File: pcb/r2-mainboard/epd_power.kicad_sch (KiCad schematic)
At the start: 79 parts, among them Q1 AO3401A, Q2 S8050, Q6 AO3400A, Q7 AO3401A, Q8 AO3401A, U23 LGS6302B5, U24 LGS6302B5, U26 LGS5145, U31 LM321, U6 MT9700, U7 TPS22914BYFPR, U8 TPS22914BYFPR, U9 LGS5145

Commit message: R2: the six approved edits, and one of them was already done
Owner-approved 2026-08-19, KiCad closed for the pass.

1. R225 22k -> 20.5K/1%, LCSC C57105 (0402WGF2052TCE, UNI-ROYAL, the
   family the rest of the board already uses). Rendered and checked:
   R224 390k over R225 20.5k with R213 100k injecting VGH_DAC, so
   20.5||100 = 17.01k and VGH = 1.2 x (1 + 390/17.01) = 28.71 V at
   DAC = 0 -- exactly epd-port.md 10.3's target.
2. The five sense-divider caps that carried codes for the wrong
   capacitance -> C1523 (0402B102K500NT, 1 nF 50 V X7R, JLC Basic,
   5.3 M stock). One part covers both the 25 V and 50 V positions.
2b. R88/R224 -> C54920667 (HRC0402F3903DNTO, 390k 1%, 20 k stock).
   C25782 had 14 units against two per board. The owner found this one;
   both obvious alternatives were traps -- C23150 is 0603, and C44937
   is 3.9 ohm despite "390K" in its part number.
3. C147 set DNP rather than deleted. panel.md 7 had already ruled that
   J6.7/J6.44 stay; that covered the pins but not the capacitor on the
   dead net. DNP drops it from placement, keeps the topology of a frozen
   sheet untouched, and leaves the footprint if a future panel drives
   the rail. in_bom stays yes -- that is this board's convention for all
   13 DNP parts, so they show up flagged rather than vanishing.
4. Ten duplicate #PWR references renumbered to #PWR1112-1121 on the
   battery sheet, which was the colliding side in every case.
5. J3 was already deleted on 2026-08-15. No work needed.
6. Specter -> Reflow across 22 files: 14 sheets, 7 generators, the
   project file. .history/ deliberately untouched.

Verified as one change: netlist before and after has 518 nets with
identical pin membership, and epd_power and epd were rendered to PNG and
inspected.

Docs updated to match: epd-port.md 10 is applied rather than designed,
frontlight.md 1 loses the "9 in series is inferred" hedge (the vendor
listing confirms 2 x 9), and io-expansion.md 4's "only guess on this
sheet" is resolved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
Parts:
- R224, R88: LCSC C25782 -> C54920667; MPN 0402WGF3903TCE -> HRC0402F3903DNTO; Manufacturer UNI-ROYAL -> HWA CHN
- R225: value 22K/1% -> 20.5K/1%; LCSC C25768 -> C57105; MPN 0402WGF2202TCE -> 0402WGF2052TCE
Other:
- title: Glider-R2 / Specter mainboard -> Glider-R2 / Reflow mainboard
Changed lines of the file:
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@@
 	(paper "A4")
 	(title_block
-		(title "Glider-R2 / Specter mainboard")
+		(title "Glider-R2 / Reflow mainboard")
 		(date "2026-08-07")
 		(rev "A")
@@
 			)
 		)
-		(property "LCSC" "C25782"
+		(property "LCSC" "C54920667"
 			(at 139.7 80.01 0)
 			(hide yes)
@@
 			)
 		)
-		(property "Manufacturer" "UNI-ROYAL"
+		(property "Manufacturer" "HWA CHN"
 			(at 0 0 0)
 			(hide yes)
@@
 			)
 		)
-		(property "MPN" "0402WGF3903TCE"
+		(property "MPN" "HRC0402F3903DNTO"
 			(at 0 0 0)
 			(hide yes)
@@
 			)
 		)
-		(property "LCSC" "C25782"
+		(property "LCSC" "C54920667"
 			(at 137.16 115.57 0)
 			(hide yes)
@@
 			)
 		)
-		(property "Manufacturer" "UNI-ROYAL"
+		(property "Manufacturer" "HWA CHN"
 			(at 0 0 0)
 			(hide yes)
@@
 			)
 		)
-		(property "MPN" "0402WGF3903TCE"
+		(property "MPN" "HRC0402F3903DNTO"
 			(at 0 0 0)
 			(hide yes)
@@
 			)
 		)
-		(property "Value" "22K/1%"
+		(property "Value" "20.5K/1%"
 			(at 142.24 124.46 0)
 			(show_name no)
@@
 			)
 		)
-		(property "LCSC" "C25768"
+		(property "LCSC" "C57105"
 			(at 137.16 123.19 0)
 			(hide yes)
@@
 			)
 		)
-		(property "MPN" "0402WGF2202TCE"
+		(property "MPN" "0402WGF2052TCE"
 			(at 0 0 0)
 			(hide yes)

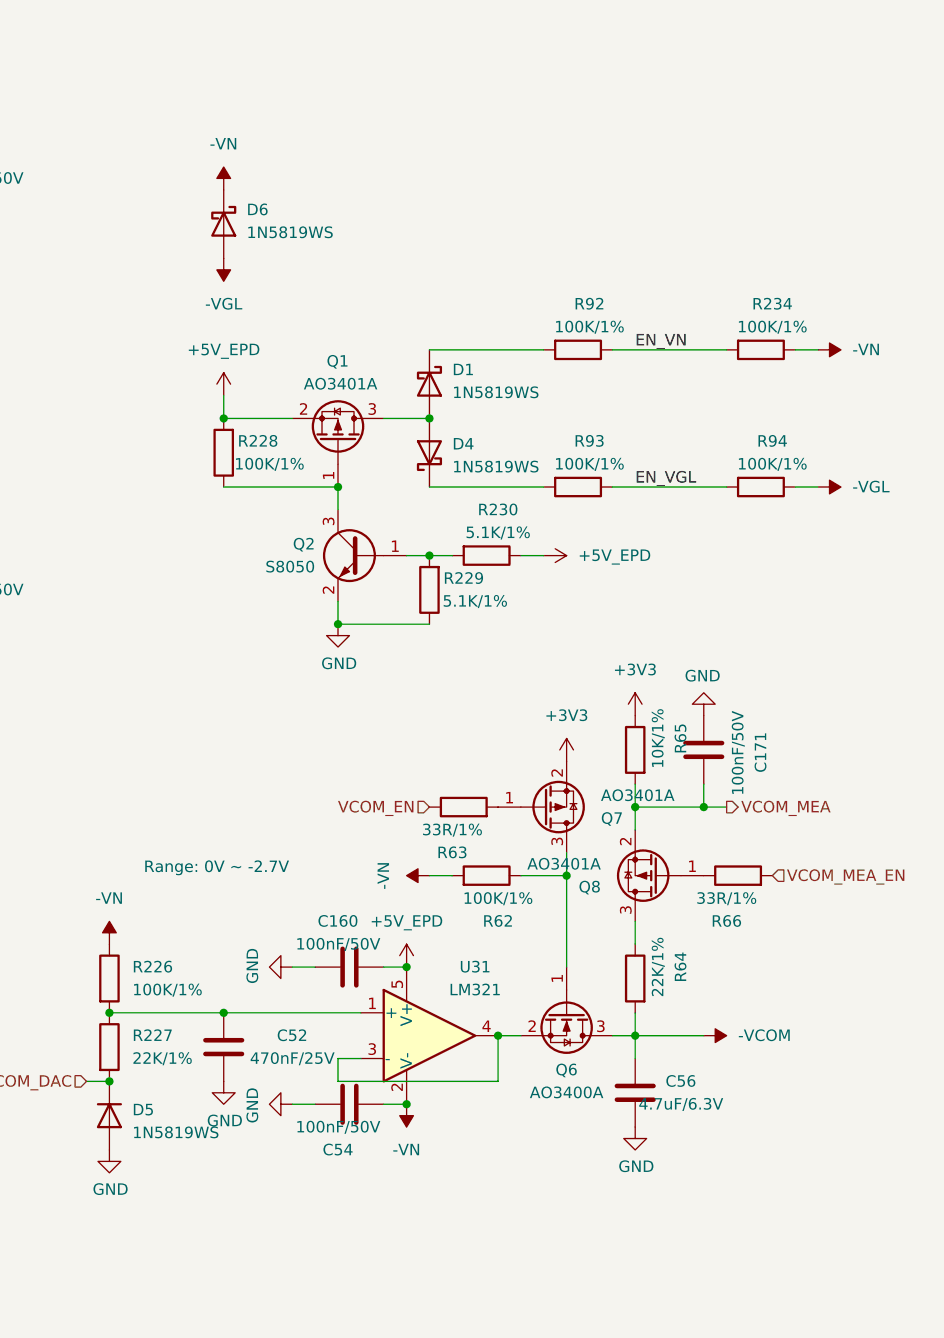
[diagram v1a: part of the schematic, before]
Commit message: Touch decided: I2C hand-wired for the prototype; Caster bitgen applied
Good Display's answer of 2026-08-31 closes the on-board GT9110H idea:
the driving board is another customer's design and they will not share
files, so the panel's ITO channel map is unobtainable at prototype
scale. The production path is now priced instead -- US$750 tooling,
MOQ 1000/lot, for a custom panel with the interface and touch IC of our
choosing.

Owner's decision: option C. Touch runs over I2C on J22, hand-wired to
the vendor board's test points for the prototype. USB was rejected --
USB0 is the charge port and USB1 is now the host port, so USB touch
would have needed a hub and would have cost touch-to-wake permanently.
No schematic change: J22/J23 and U54/U55 stay exactly as drawn, DNP.

io-expansion.md 5.2 records the decision and the three firmware ways to
disable touch-to-wake; 5.3 records a real gap found on the vendor board
-- it exposes SDA/SCL/VDD/GND/DBG/INT/DP and *no* RST pad, so reset
becomes a power cycle through MCU_EN_TOUCH, and the GT9110's I2C
address cannot be selected and must be scanned for at bring-up.

Also in this commit, the owner's work: Caster bitgen at ConfigRate 22 /
x4 / binary (submodule pointer bump), epd_power and io_expansion sheet
edits, and board layout.

Co-Authored-By: Claude Opus 5 <noreply@anthropic.com>
Claude-Session: https://claude.ai/code/session_01MHTAe6ZnhogTEgtyPcLhwG
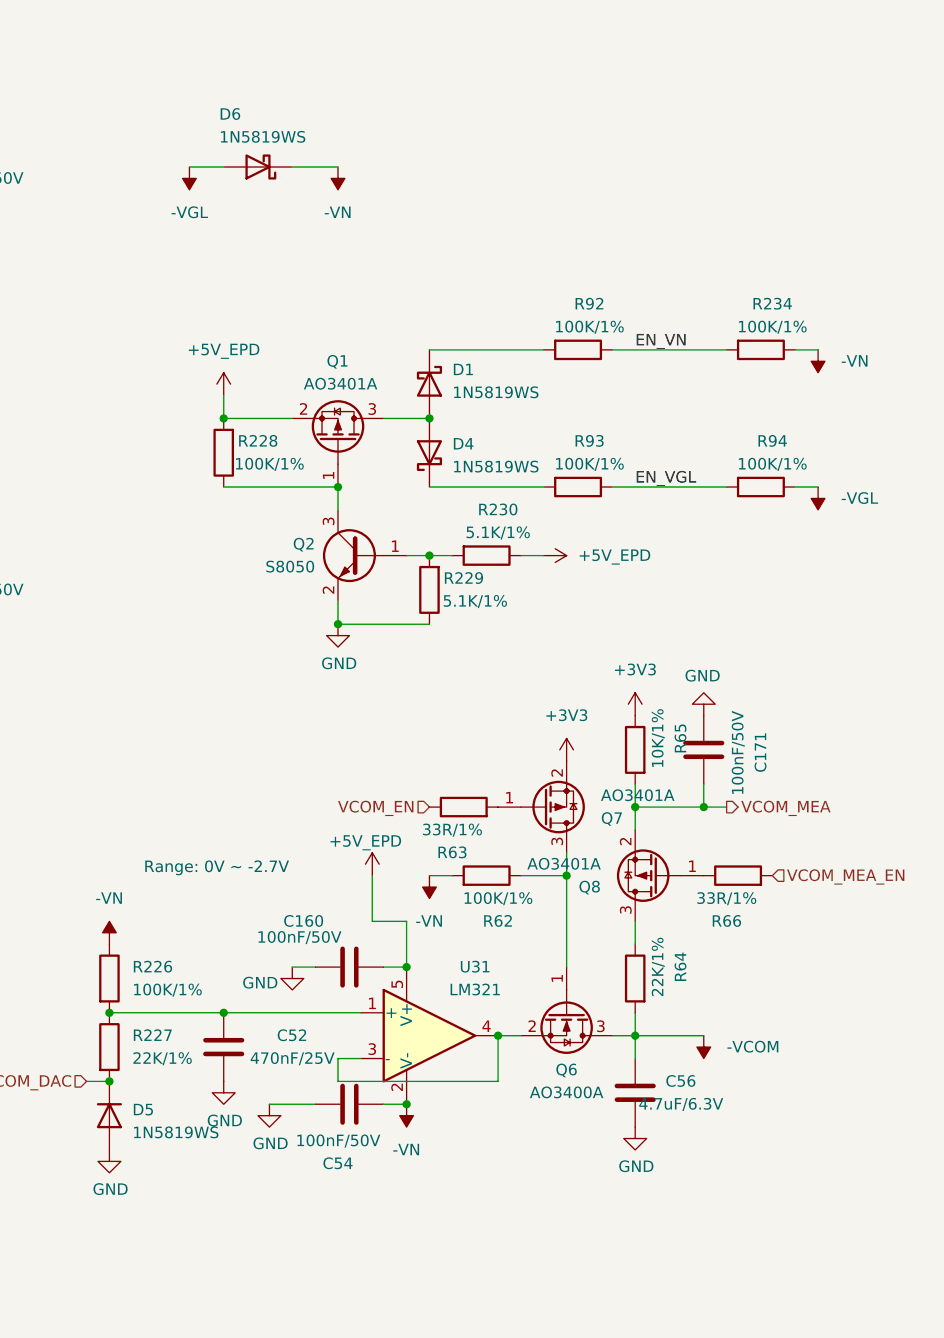
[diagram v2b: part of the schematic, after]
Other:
- moved on the sheet: D6

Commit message: R2: renumber every sheet to the page-based designator scheme
The owner's scheme is classifier + sheet page + two-digit part from 00. Four
sheets already used it; this converts the remaining nine, so all thirteen now
agree: pages 2-9 take three digits, pages 10-14 four. 292 of 333 designators
changed. A part shared by several sheets takes its lowest page, so the FPGA is
U700 (pages 7-9) and the two SoM connectors are J501/J502 (pages 5-6).

The whole risk here is silently rewiring the board, so the netlist was diffed
rather than eyeballed:

  nets 519 -> 519, total pin connections 1563 -> 1563
  named nets present in both whose pin multiset changed: 0
  ERC unchanged at 14 errors / 20 warnings
  check_ucf.py: 99 balls matched, 0 failures

That last one matters most: it resolves the gateware's 113 UCF constraints to
board nets *by ball name*, so it is the sharpest detector of the corruption
this change could cause.

Two earlier attempts did cause exactly that. A bare quoted-string substitution
also rewrites FPGA ball names (C1, D2, N11, T1) and BTH-060 pin names (A1-D60),
which are spelled exactly like designators; one run left ERC identical while 40
nets came back with a different pin multiset. The tool now substitutes only at
the two positions that store an instance's designator, and excludes every pin
name everywhere else. docs/layout.md 9.5 records the hazard and how to prove a
renumber was clean.

Only the three scripts that read the design are updated. The gen_*/patch_*/
port_r1.py scripts keep the old names deliberately: each wrote a sheet once and
has not been re-runnable since it was hand-edited in Eeschema, so they are a
historical record -- and port_r1.py's dict keys are R1 designators that were
never renumbered at all.

Co-Authored-By: Claude Opus 5 <noreply@anthropic.com>
Claude-Session: https://claude.ai/code/session_01MHTAe6ZnhogTEgtyPcLhwG
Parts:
- renumbered C17 to C1100, C35 to C1101, C37 to C1102, C38 to C1103, C51 to C1104, C52 to C1105, C53 to C1106, C54 to C1107, C56 to C1108, C104 to C1109, C160 to C1110, C165 to C1111, C166 to C1112, C167 to C1113, C171 to C1114, C172 to C1115, C173 to C1116, C174 to C1117, C175 to C1118, C176 to C1119, C177 to C1120, C178 to C1121, C232 to C1122, C233 to C1123, C241 to C1124, C242 to C1125, C244 to C1126, C245 to C1127, C246 to C1128, C249 to C1129, D1 to D1100, D2 to D1101, D3 to D1102, D4 to D1103, D5 to D1104, D6 to D1105, D15 to D1106, D17 to D1107, L5 to L1100, L6 to L1101, L30 to L1102, L32 to L1103, Q1 to Q1100, Q2 to Q1101, Q6 to Q1102, Q7 to Q1103, Q8 to Q1104, R62 to R1100, R63 to R1101, R64 to R1102, R65 to R1103, R66 to R1104, R78 to R1105, R79 to R1106, R88 to R1107, R89 to R1108, R92 to R1109, R93 to R1110, R94 to R1111, R213 to R1112, R217 to R1113, R218 to R1114, R219 to R1115, R224 to R1116, R225 to R1117, R226 to R1118, R227 to R1119, R228 to R1120, R229 to R1121, R230 to R1122, R234 to R1123, U6 to U1100, U7 to U1101, U8 to U1102, U9 to U1103, U23 to U1104, U24 to U1105, U26 to U1106, U31 to U1107
